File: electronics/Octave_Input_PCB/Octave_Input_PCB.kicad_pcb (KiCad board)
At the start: 2 copper layers, 87.8 x 95.8 mm, 64 parts, among them J1 HRO_TYPE-C-31-M-12, SW1 SW_Hot_Swap_Socket, SW10 SW_Hot_Swap_Socket, SW11 SW_Hot_Swap_Socket, SW12 SW_Hot_Swap_Socket, SW13 SW_Hot_Swap_Socket, SW14 Alps_Alpine_RKJXV1224, SW15 Bourns_PEC12R-4xxxF-Sxxx, SW2 SW_Hot_Swap_Socket, SW3 SW_Hot_Swap_Socket, SW4 SW_Hot_Swap_Socket, SW5 SW_Hot_Swap_Socket, SW6 SW_Hot_Swap_Socket, SW7 SW_Hot_Swap_Socket, SW8 SW_Hot_Swap_Socket, SW9 SW_Hot_Swap_Socket, U1 AP2112K-3.3, U2 Raspberry_Pi_RP2040, U3 W25Q64JVSS, Y1 12MHz

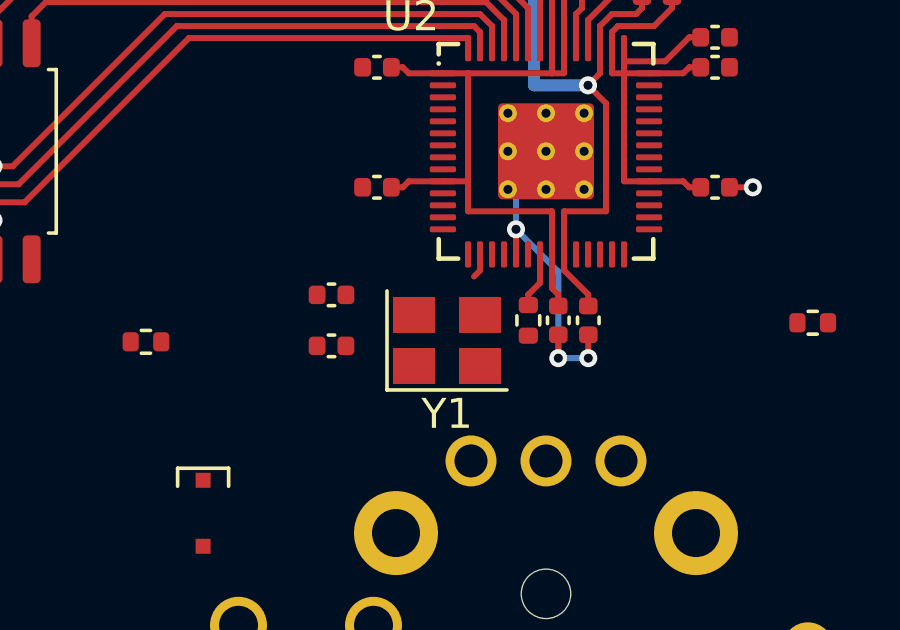
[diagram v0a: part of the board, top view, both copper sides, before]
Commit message: Update Octave_Input_PCB.kicad_pcb
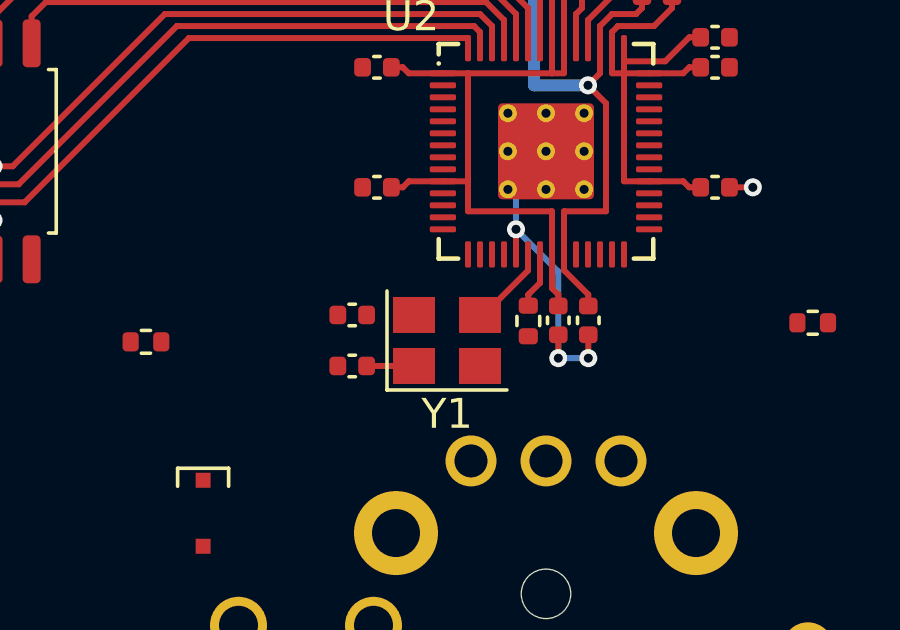
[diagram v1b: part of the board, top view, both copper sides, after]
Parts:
- moved C15 0.96 mm to (79.3, 110.2)
- moved C16 0.96 mm to (79.3, 111.9)
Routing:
- net Net-(C15-Pad1): track 0.00 -> 2.75 mm
- net Net-(C16-Pad1): track 0.00 -> 1.58 mm
- net unconnected-(U2-Pad16): track 0.82 -> 0.00 mm

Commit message: [WIP] Update schematic and PCB
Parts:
- added SW21: Alps_Alpine_SKRP, Octave_Library:Tactile_Switch_SKRP_ Series, F.Cu at (100.0, 109.5)
- added SW22: Alps_Alpine_SKRP, Octave_Library:Tactile_Switch_SKRP_ Series, F.Cu at (71.4, 109.5)
- moved R6 5.08 mm to (72.4, 106.0)
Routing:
- added copper zone on B.Cu, net GND
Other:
- board text added: "BOOT"
- board text added: "RESET"
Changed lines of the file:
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@@
   (title_block
     (title "Octave - Input PCB")
-    (date "2022-05-08")
+    (date "2022-05-21")
     (rev "5.a")
     (comment 4 "https://github.com/takayoshiotake/octave-12-key-macropad")
@@
     )
   )
+  (footprint "Octave_Library:Tactile_Switch_SKRP_ Series" (layer "F.Cu")
+    (at 100.0125 109.5375 90)
+    (property "Sheetfile" "Octave_Input_PCB.kicad_sch")
+    (property "Sheetname" "")
+    (attr smd)
+    (fp_text reference "SW21" (at 0 -2.54 90 unlocked) (layer "F.SilkS") hide
+      (effects (font (size 1 1) (thickness 0.15)))
+    )
+    (fp_text value "Alps_Alpine_SKRP" (at 0 2.54 90 unlocked) (layer "F.Fab") hide
+      (effects (font (size 1 1) (thickness 0.15)))
+    )
+    (fp_text user "${REFERENCE}" (at 0 4.445 90 unlocked) (layer "F.Fab") hide
+      (effects (font (size 1 1) (thickness 0.15)))
+    )
+    (fp_rect (start -2.8 -1.8) (end 2.8 1.8) (layer "Margin") (width 0.05) (fill none))
+    (fp_line (start -0.4 1.1) (end 0.4 1.1) (layer "F.Fab") (width 0.1))
+    (fp_line (start -0.4 -1.1) (end 0.4 -1.1) (layer "F.Fab") (width 0.1))
+    (fp_rect (start -2.1 -1.6) (end 2.1 1.6) (layer "F.Fab") (width 0.1) (fill none))
+    (fp_arc (start 0.4 -1.1) (mid 1.5 0) (end 0.4 1.1) (layer "F.Fab") (width 0.1))
+    (fp_arc (start -0.4 1.1) (mid -1.5 0) (end -0.4 -1.1) (layer "F.Fab") (width 0.1))
+    (pad "1" smd rect (at -2.075 -1.075 90) (size 1.05 0.65) (layers "F.Cu" "F.Paste" "F.Mask")
+      (net 28 "GND") (pinfunction "1") (pintype "passive"))
+    (pad "2" smd rect (at 2.075 -1.075 90) (size 1.05 0.65) (layers "F.Cu" "F.Paste" "F.Mask")
+      (net 87 "~{RESET}") (pinfunction "2") (pintype "passive"))
+    (pad "3" smd rect (at -2.075 1.075 90) (size 1.05 0.65) (layers "F.Cu" "F.Paste" "F.Mask")
+      (net 28 "GND") (pinfunction "3") (pintype "passive"))
+    (pad "4" smd rect (at 2.075 1.075 90) (size 1.05 0.65) (layers "F.Cu" "F.Paste" "F.Mask")
+      (net 87 "~{RESET}") (pinfunction "4") (pintype "passive"))
+  )
   (footprint "Capacitor_SMD:C_0402_1005Metric" (layer "F.Cu")
     (at 83.925 97.74 90)
@@
     )
   )
+  (footprint "Octave_Library:Tactile_Switch_SKRP_ Series" (layer "F.Cu")
+    (at 71.4375 109.5375 90)
+    (property "Sheetfile" "Octave_Input_PCB.kicad_sch")
+    (property "Sheetname" "")
+    (attr smd)
+    (fp_text reference "SW22" (at 0 -2.54 90 unlocked) (layer "F.SilkS") hide
+      (effects (font (size 1 1) (thickness 0.15)))
+    )
+    (fp_text value "Alps_Alpine_SKRP" (at 0 2.54 90 unlocked) (layer "F.Fab") hide
+      (effects (font (size 1 1) (thickness 0.15)))
+    )
+    (fp_text user "${REFERENCE}" (at 0 4.445 90 unlocked) (layer "F.Fab") hide
+      (effects (font (size 1 1) (thickness 0.15)))
+    )
+    (fp_rect (start -2.8 -1.8) (end 2.8 1.8) (layer "Margin") (width 0.05) (fill none))
+    (fp_line (start -0.4 1.1) (end 0.4 1.1) (layer "F.Fab") (width 0.1))
+    (fp_line (start -0.4 -1.1) (end 0.4 -1.1) (layer "F.Fab") (width 0.1))
+    (fp_rect (start -2.1 -1.6) (end 2.1 1.6) (layer "F.Fab") (width 0.1) (fill none))
+    (fp_arc (start 0.4 -1.1) (mid 1.5 0) (end 0.4 1.1) (layer "F.Fab") (width 0.1))
+    (fp_arc (start -0.4 1.1) (mid -1.5 0) (end -0.4 -1.1) (layer "F.Fab") (width 0.1))
+    (pad "1" smd rect (at -2.075 -1.075 90) (size 1.05 0.65) (layers "F.Cu" "F.Paste" "F.Mask")
+      (net 28 "GND") (pinfunction "1") (pintype "passive"))
+    (pad "2" smd rect (at 2.075 -1.075 90) (size 1.05 0.65) (layers "F.Cu" "F.Paste" "F.Mask")
+      (net 86 "~{USB_BOOT}") (pinfunction "2") (pintype "passive"))
+    (pad "3" smd rect (at -2.075 1.075 90) (size 1.05 0.65) (layers "F.Cu" "F.Paste" "F.Mask")
+      (net 28 "GND") (pinfunction "3") (pintype "passive"))
+    (pad "4" smd rect (at 2.075 1.075 90) (size 1.05 0.65) (layers "F.Cu" "F.Paste" "F.Mask")
+      (net 86 "~{USB_BOOT}") (pinfunction "4") (pintype "passive"))
+  )
   (footprint "Octave_Library:D_SOD-323F" (layer "F.Cu")
     (at 111.1758 57.15 90)
@@
     (property "Sheetname" "")
     (attr smd)
-    (fp_text reference "U1" (at 0 -2.4 90) (layer "F.SilkS")
+    (fp_text reference "U1" (at 0 2.4 90) (layer "F.SilkS")
       (effects (font (size 1 1) (thickness 0.15)))
     )
-    (fp_text value "AP2112K-3.3" (at 0 2.4 90) (layer "F.Fab")
+    (fp_text value "AP2112K-3.3" (at 0 2.4 90) (layer "F.Fab") hide
       (effects (font (size 1 1) (thickness 0.15)))
     )
@@
   )
   (footprint "Resistor_SMD:R_0402_1005Metric" (layer "F.Cu")
-    (at 72.39 111.125)
+    (at 72.39 106.045)
     (descr "Resistor SMD 0402 (1005 Metric), square (rectangular) end terminal, IPC_7351 nominal, (Body size source: IPC-SM-782 page 72, https://www.pcb-3d.com/wordpress/wp-content/uploads/ipc-sm-782a_amendment_1_and_2.pdf), generated with kicad-footprint-generator")
     (tags "resistor")
@@
     (effects (font (size 1 1) (thickness 0.15)) (justify left))
   )
+  (gr_text "RESET" (at 100.0125 113.1375) (layer "F.SilkS")
+    (effects (font (size 1 1) (thickness 0.15)))
+  )
+  (gr_text "BOOT" (at 71.4375 113.1375) (layer "F.SilkS")
+    (effects (font (size 1 1) (thickness 0.15)))
+  )
   (dimension (type aligned) (layer "Cmts.User")
     (pts (xy 49.625 49.625) (xy 44.109567 44.109567))
@@
   (segment (start 85.525 108.2125) (end 85.525 109.16) (width 0.2) (layer "F.Cu") (net 85))
   (segment (start 85.525 109.16) (end 85.135 109.55) (width 0.2) (layer "F.Cu") (net 85))
+  (zone (net 28) (net_name "GND") (layer "B.Cu") (name "GND") (hatch edge 0.508)
+    (connect_pads (clearance 0))
+    (min_thickness 0.254) (filled_areas_thickness no)
+    (fill (thermal_gap 0.508) (thermal_bridge_width 0.508))
+    (polygon
+      (pts
+        (xy 129.6 137.6)
+        (xy 41.8 137.6)
+        (xy 41.8 41.8)
+        (xy 129.6 41.8)
+      )
+    )
+  )
 )

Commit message: [WIP] Update PCB
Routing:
- net GND: track 46.8 -> 52.7 mm, vias 10 -> 15
- net Net-(C16-Pad1): track 1.58 -> 6.03 mm
- net Net-(J1-PadA7): track 48.7 -> 52.4 mm
- net Net-(J1-PadA6): track 50.0 -> 53.5 mm
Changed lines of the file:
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@@
   (title_block
     (title "Octave - Input PCB")
-    (date "2022-05-21")
+    (date "2022-05-23")
     (rev "5.a")
     (comment 4 "https://github.com/takayoshiotake/octave-12-key-macropad")
@@
       (effects (font (size 1 1) (thickness 0.15)))
     )
-    (fp_rect (start -2.8 -1.8) (end 2.8 1.8) (layer "Margin") (width 0.05) (fill none))
+    (fp_rect (start -2.8 -1.8) (end 2.8 1.8) (layer "F.CrtYd") (width 0.05) (fill none))
     (fp_line (start -0.4 1.1) (end 0.4 1.1) (layer "F.Fab") (width 0.1))
     (fp_line (start -0.4 -1.1) (end 0.4 -1.1) (layer "F.Fab") (width 0.1))
     (fp_rect (start -2.1 -1.6) (end 2.1 1.6) (layer "F.Fab") (width 0.1) (fill none))
-    (fp_arc (start 0.4 -1.1) (mid 1.5 0) (end 0.4 1.1) (layer "F.Fab") (width 0.1))
     (fp_arc (start -0.4 1.1) (mid -1.5 0) (end -0.4 -1.1) (layer "F.Fab") (width 0.1))
+    (fp_arc (start 0.4 -1.1) (mid 1.5 0) (end 0.4 1.1) (layer "F.Fab") (width 0.1))
     (pad "1" smd rect (at -2.075 -1.075 90) (size 1.05 0.65) (layers "F.Cu" "F.Paste" "F.Mask")
       (net 28 "GND") (pinfunction "1") (pintype "passive"))
@@
       (effects (font (size 1 1) (thickness 0.15)))
     )
-    (fp_rect (start -2.8 -1.8) (end 2.8 1.8) (layer "Margin") (width 0.05) (fill none))
-    (fp_line (start -0.4 1.1) (end 0.4 1.1) (layer "F.Fab") (width 0.1))
+    (fp_rect (start -2.8 -1.8) (end 2.8 1.8) (layer "F.CrtYd") (width 0.05) (fill none))
     (fp_line (start -0.4 -1.1) (end 0.4 -1.1) (layer "F.Fab") (width 0.1))
+    (fp_line (start -0.4 1.1) (end 0.4 1.1) (layer "F.Fab") (width 0.1))
     (fp_rect (start -2.1 -1.6) (end 2.1 1.6) (layer "F.Fab") (width 0.1) (fill none))
     (fp_arc (start 0.4 -1.1) (mid 1.5 0) (end 0.4 1.1) (layer "F.Fab") (width 0.1))
@@
     )
   )
-  (footprint "Crystal:Crystal_SMD_3225-4Pin_3.2x2.5mm" locked (layer "F.Cu")
+  (footprint "Crystal:Crystal_SMD_3225-4Pin_3.2x2.5mm" (layer "F.Cu")
     (at 82.425 111.08)
     (descr "SMD Crystal SERIES SMD3225/4 http://www.txccrystal.com/images/pdf/7m-accuracy.pdf, 3.2x2.5mm^2 package")
@@
   (segment (start 111.1758 112.1858) (end 111.1758 113.25) (width 0.25) (layer "F.Cu") (net 25))
   (segment (start 82.3125 59.4) (end 82.315 59.4025) (width 0.2) (layer "F.Cu") (net 28))
+  (segment (start 83.925 97.26) (end 83.925 96.48) (width 0.2) (layer "F.Cu") (net 28))
   (segment (start 91.84 105.975) (end 92.619999 105.975) (width 0.2) (layer "F.Cu") (net 28))
   (segment (start 88.975 48.2205) (end 88.975 49.445499) (width 0.2) (layer "F.Cu") (net 28))
@@
   (segment (start 81.535 59.4) (end 82.3125 59.4) (width 0.2) (layer "F.Cu") (net 28))
   (segment (start 83.975 50.6355) (end 83.975 51.4055) (width 0.2) (layer "F.Cu") (net 28))
+  (segment (start 85.925 96.48) (end 85.925 97.26) (width 0.2) (layer "F.Cu") (net 28))
   (segment (start 87.135 110.89) (end 87.135 111.669999) (width 0.2) (layer "F.Cu") (net 28))
   (segment (start 81.535 64.4225) (end 82.315 64.4225) (width 0.2) (layer "F.Cu") (net 28))
+  (segment (start 78.005 111.93) (end 78.785 111.93) (width 0.2) (layer "F.Cu") (net 28))
+  (segment (start 78.785 110.23) (end 78.005 110.23) (width 0.2) (layer "F.Cu") (net 28))
   (segment (start 86.975 50.6355) (end 86.975 51.4055) (width 0.2) (layer "F.Cu") (net 28))
   (segment (start 82.325 60.775) (end 82.325 59.4125) (width 0.2) (layer "F.Cu") (net 28))
   (segment (start 86.135 110.89) (end 86.135 111.669999) (width 0.2) (layer "F.Cu") (net 28))
   (segment (start 82.475 49.445499) (end 82.475 48.2205) (width 0.2) (layer "F.Cu") (net 28))
+  (segment (start 84.925 97.26) (end 84.925 96.48) (width 0.2) (layer "F.Cu") (net 28))
+  (via (at 83.925 96.48) (size 0.6) (drill 0.3) (layers "F.Cu" "B.Cu") (remove_unused_layers) (keep_end_layers) (net 28))
+  (via (at 78.005 111.93) (size 0.6) (drill 0.3) (layers "F.Cu" "B.Cu") (remove_unused_layers) (keep_end_layers) (net 28))
   (via (at 83.975 51.4055) (size 0.6) (drill 0.3) (layers "F.Cu" "B.Cu") (remove_unused_layers) (keep_end_layers) (net 28))
+  (via (at 84.925 96.48) (size 0.6) (drill 0.3) (layers "F.Cu" "B.Cu") (remove_unused_layers) (keep_end_layers) (net 28))
   (via (at 87.135 111.669999) (size 0.6) (drill 0.3) (layers "F.Cu" "B.Cu") (remove_unused_layers) (keep_end_layers) (net 28))
   (via (at 81.535 64.4225) (size 0.6) (drill 0.3) (layers "F.Cu" "B.Cu") (remove_unused_layers) (keep_end_layers) (net 28))
   (via (at 92.619999 105.975) (size 0.6) (drill 0.3) (layers "F.Cu" "B.Cu") (remove_unused_layers) (keep_end_layers) (net 28))
   (via (at 88.975 49.445499) (size 0.6) (drill 0.3) (layers "F.Cu" "B.Cu") (remove_unused_layers) (keep_end_layers) (net 28))
+  (via (at 85.925 96.48) (size 0.6) (drill 0.3) (layers "F.Cu" "B.Cu") (remove_unused_layers) (keep_end_layers) (net 28))
   (via (at 86.135 111.669999) (size 0.6) (drill 0.3) (layers "F.Cu" "B.Cu") (remove_unused_layers) (keep_end_layers) (net 28))
+  (via (at 78.005 110.23) (size 0.6) (drill 0.3) (layers "F.Cu" "B.Cu") (remove_unused_layers) (keep_end_layers) (net 28))
   (via (at 84.725 107.375) (size 0.6) (drill 0.3) (layers "F.Cu" "B.Cu") (remove_unused_layers) (keep_end_layers) (net 28))
   (via (at 81.535 59.4) (size 0.6) (drill 0.3) (layers "F.Cu" "B.Cu") (remove_unused_layers) (keep_end_layers) (net 28))
@@
   (segment (start 82.475 49.445499) (end 83.954501 49.445499) (width 0.2) (layer "B.Cu") (net 28))
   (segment (start 84.725 107.375) (end 84.725 106.315) (width 0.2) (layer "B.Cu") (net 28))
+  (segment (start 85.925 96.48) (end 83.925 96.48) (width 0.2) (layer "B.Cu") (net 28))
   (segment (start 81.535 59.4) (end 82.475 59.4) (width 0.2) (layer "B.Cu") (net 28))
   (segment (start 83.975 51.4055) (end 86.975 51.4055) (width 0.2) (layer "B.Cu") (net 28))
@@
   (segment (start 81.535 59.4) (end 81.535 64.4225) (width 0.2) (layer "B.Cu") (net 28))
   (segment (start 86.975 49.6155) (end 86.975 48.2205) (width 0.2) (layer "F.Cu") (net 32))
+  (segment (start 86.925 97.93) (end 86.925 96.66) (width 0.2) (layer "F.Cu") (net 33))
   (segment (start 85.175 47.0955) (end 84.975 47.2955) (width 0.2) (layer "F.Cu") (net 33))
-  (segment (start 85.475 49.8455) (end 85.475 95) (width 0.2) (layer "F.Cu") (net 33))
+  (segment (start 86.925 96.66) (end 85.475 95.21) (width 0.2) (layer "F.Cu") (net 33))
   (segment (start 85.775 47.0955) (end 85.975 47.2955) (width 0.2) (layer "F.Cu") (net 33))
   (segment (start 85.775 47.0955) (end 85.175 47.0955) (width 0.2) (layer "F.Cu") (net 33))
-  (segment (start 84.975 48.2205) (end 84.975 49.3455) (width 0.2) (layer "F.Cu") (net 33))
   (segment (start 84.975 48.2205) (end 84.975 47.2955) (width 0.2) (layer "F.Cu") (net 33))
+  (segment (start 85.475 95.21) (end 85.475 49.8455) (width 0.2) (layer "F.Cu") (net 33))
   (segment (start 85.975 47.2955) (end 85.975 48.2205) (width 0.2) (layer "F.Cu") (net 33))
-  (segment (start 84.975 49.3455) (end 85.475 49.8455) (width 0.2) (layer "F.Cu") (net 33))
+  (segment (start 85.475 49.8455) (end 84.975 49.3455) (width 0.2) (layer "F.Cu") (net 33))
+  (segment (start 84.975 49.3455) (end 84.975 48.2205) (width 0.2) (layer "F.Cu") (net 33))
   (segment (start 85.475 49.1455) (end 85.475 48.2205) (width 0.2) (layer "F.Cu") (net 35))
   (segment (start 85.675 49.3455) (end 86.275 49.3455) (width 0.2) (layer "F.Cu") (net 35))
+  (segment (start 85.975 49.3455) (end 85.975 94.71) (width 0.2) (layer "F.Cu") (net 35))
   (segment (start 85.675 49.3455) (end 85.475 49.1455) (width 0.2) (layer "F.Cu") (net 35))
+  (segment (start 87.925 96.66) (end 87.925 97.93) (width 0.2) (layer "F.Cu") (net 35))
   (segment (start 86.475 48.2205) (end 86.475 49.1455) (width 0.2) (layer "F.Cu") (net 35))
+  (segment (start 85.975 94.71) (end 87.925 96.66) (width 0.2) (layer "F.Cu") (net 35))
   (segment (start 86.275 49.3455) (end 86.475 49.1455) (width 0.2) (layer "F.Cu") (net 35))
-  (segment (start 85.975 95) (end 85.975 49.3455) (width 0.2) (layer "F.Cu") (net 35))
   (segment (start 83.975 49.6155) (end 83.975 48.2205) (width 0.2) (layer "F.Cu") (net 36))
   (segment (start 86.325 108.74) (end 86.325 108.2125) (width 0.2) (layer "F.Cu") (net 38))
@@
   (segment (start 83.525 110.23) (end 83.645 110.23) (width 0.2) (layer "F.Cu") (net 83))
   (segment (start 85.125 108.2125) (end 85.125 108.75) (width 0.2) (layer "F.Cu") (net 83))
+  (segment (start 82.6 111.08) (end 81.75 111.93) (width 0.2) (layer "F.Cu") (net 84))
+  (segment (start 82.6 111.08) (end 84.995 111.08) (width 0.2) (layer "F.Cu") (net 84))
+  (segment (start 81.75 111.93) (end 81.325 111.93) (width 0.2) (layer "F.Cu") (net 84))
+  (segment (start 84.995 111.08) (end 85.135 110.94) (width 0.2) (layer "F.Cu") (net 84))
+  (segment (start 85.135 110.94) (end 84.971511 111.103489) (width 0.2) (layer "F.Cu") (net 84))
   (segment (start 81.325 111.93) (end 79.745 111.93) (width 0.2) (layer "F.Cu") (net 84))
   (segment (start 85.135 109.92) (end 85.135 109.55) (width 0.2) (layer "F.Cu") (net 85))
@@
     (connect_pads (clearance 0))
     (min_thickness 0.254) (filled_areas_thickness no)
-    (fill (thermal_gap 0.508) (thermal_bridge_width 0.508))
+    (fill yes (thermal_gap 0.508) (thermal_bridge_width 0.508))
     (polygon
       (pts

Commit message: [WIP] Update schematic and PCB
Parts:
- moved R6 8.18 mm to (65.3, 110.1)
- moved R5 6.48 mm to (88.1, 110.4), turned to 90 degrees
- moved D15 3.81 mm to (57.1, 114.3), turned to 90 degrees
- moved D14 1.23 mm to (75.5, 116.5)
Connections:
- SW14 pad 1: Net-(D14-Pad2) -> col2
- SW14 pad 2: col2 -> Net-(D14-Pad2)
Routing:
- net ~{USB_BOOT}: track 0.00 -> 8.24 mm
- net Net-(C15-Pad1): track 2.75 -> 7.46 mm
- net ~{RESET}: track 0.00 -> 4.11 mm
- net GND: track 52.7 -> 55.7 mm, vias 15 -> 24
- net Net-(C16-Pad1): track 6.03 -> 7.84 mm
- net QSPI_SS_N: track 22.2 -> 23.9 mm
- net row0: track 6.65 -> 5.96 mm

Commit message: [WIP] Update schematic and PCB
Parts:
- C21, C22: value 0.01u -> 0.01uF; footprint Octave_Library:C_0805_2012Metric -> Capacitor_SMD:C_0402_1005Metric
- R11, R12, R13, R14: footprint Octave_Library:R_0805_2012Metric -> Resistor_SMD:R_0402_1005Metric
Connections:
- C22 pad 1: GND -> A
- C22 pad 2: A -> GND
- R12 pad 1: B -> SignalB
- R12 pad 2: SignalB -> B
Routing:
- net +3V3: track 46.3 -> 97.9 mm, vias 0 -> 4
- net GND: track 55.7 -> 32.3 mm
- net Net-(D14-Pad2): track 0.00 -> 9.48 mm
- net +1V1: track 22.4 -> 23.3 mm
- added copper zone on F.Cu, net +3V3

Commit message: [WIP] Update schematic and PCB
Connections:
- R11 pad 2: SignalB -> rotaryB
- R12 pad 1: SignalB -> rotaryB
- R13 pad 2: SignalA -> rotaryA
- R14 pad 2: SignalA -> rotaryA
- SW14 pad 1: col2 -> col1
- SW14 pad 4: unconnected-(SW14-Pad4) -> stickA
- SW14 pad 7: unconnected-(SW14-Pad7) -> stickB
- U2 pad 14: unconnected-(U2-Pad14) -> NEOPIX_POWER
- U2 pad 15: unconnected-(U2-Pad15) -> NEOPIX
- U2 pad 2: unconnected-(U2-Pad2) -> col2
- U2 pad 3: unconnected-(U2-Pad3) -> col3
- U2 pad 34: unconnected-(U2-Pad34) -> col0
- U2 pad 35: unconnected-(U2-Pad35) -> col1
- U2 pad 36: unconnected-(U2-Pad36) -> row3
- U2 pad 37: unconnected-(U2-Pad37) -> row2
- U2 pad 38: unconnected-(U2-Pad38) -> stickA
- U2 pad 39: unconnected-(U2-Pad39) -> stickB
- U2 pad 4: unconnected-(U2-Pad4) -> rotaryA
- U2 pad 40: unconnected-(U2-Pad40) -> row1
- U2 pad 41: unconnected-(U2-Pad41) -> row0
- U2 pad 5: unconnected-(U2-Pad5) -> rotaryB
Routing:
- net col1: track 38.1 -> 98.1 mm
- net +3V3: track 97.9 -> 136.6 mm, vias 4 -> 6
- net row2: track 5.96 -> 44.1 mm
- net row0: track 5.96 -> 44.1 mm
- net row1: track 6.01 -> 44.1 mm
- net col3: track 38.1 -> 54.7 mm

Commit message: [WIP] Update schematic and PCB
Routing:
- net GND: track 32.3 -> 26.3 mm

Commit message: [WIP] Update schematic and PCB
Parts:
- moved R13 19.8 mm to (70.5, 119.0)
- moved D15 16.5 mm to (73.5, 116.5), turned to -90 degrees
- moved R11 15.3 mm to (68.2, 119.3)
- moved R14 8.98 mm to (64.0, 125.0)
- moved C21 8.61 mm to (51.1, 125.8)
- moved C22 6.69 mm to (63.0, 125.0)
- moved R12 4.56 mm to (52.6, 126.0)
- moved U1 2.38 mm to (82.3, 64.3)
- moved C1 2.38 mm to (82.8, 61.8)
- moved C2 2.38 mm to (82.8, 66.8)
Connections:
- U2 pad 37: row2 -> row0
- U2 pad 41: row0 -> row2
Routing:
- net row1: track 44.1 -> 99.2 mm, vias 4 -> 8
- net row2: track 44.1 -> 73.7 mm, vias 4 -> 6
- net col3: track 54.7 -> 80.9 mm, vias 0 -> 1
- net row0: track 44.1 -> 62.2 mm, vias 4 -> 6
- net col2: track 38.1 -> 55.9 mm, vias 0 -> 2
- net ~{RESET}: track 4.11 -> 15.9 mm
- net +5V: track 23.6 -> 26.0 mm
- net col1: track 98.1 -> 97.5 mm
